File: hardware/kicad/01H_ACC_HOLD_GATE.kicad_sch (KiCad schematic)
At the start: 17 parts, among them Q912 MMBT5551, Q914 PMBT5551,215, Q915 MMBT5401-7-F, U911 140356145000 HOLD

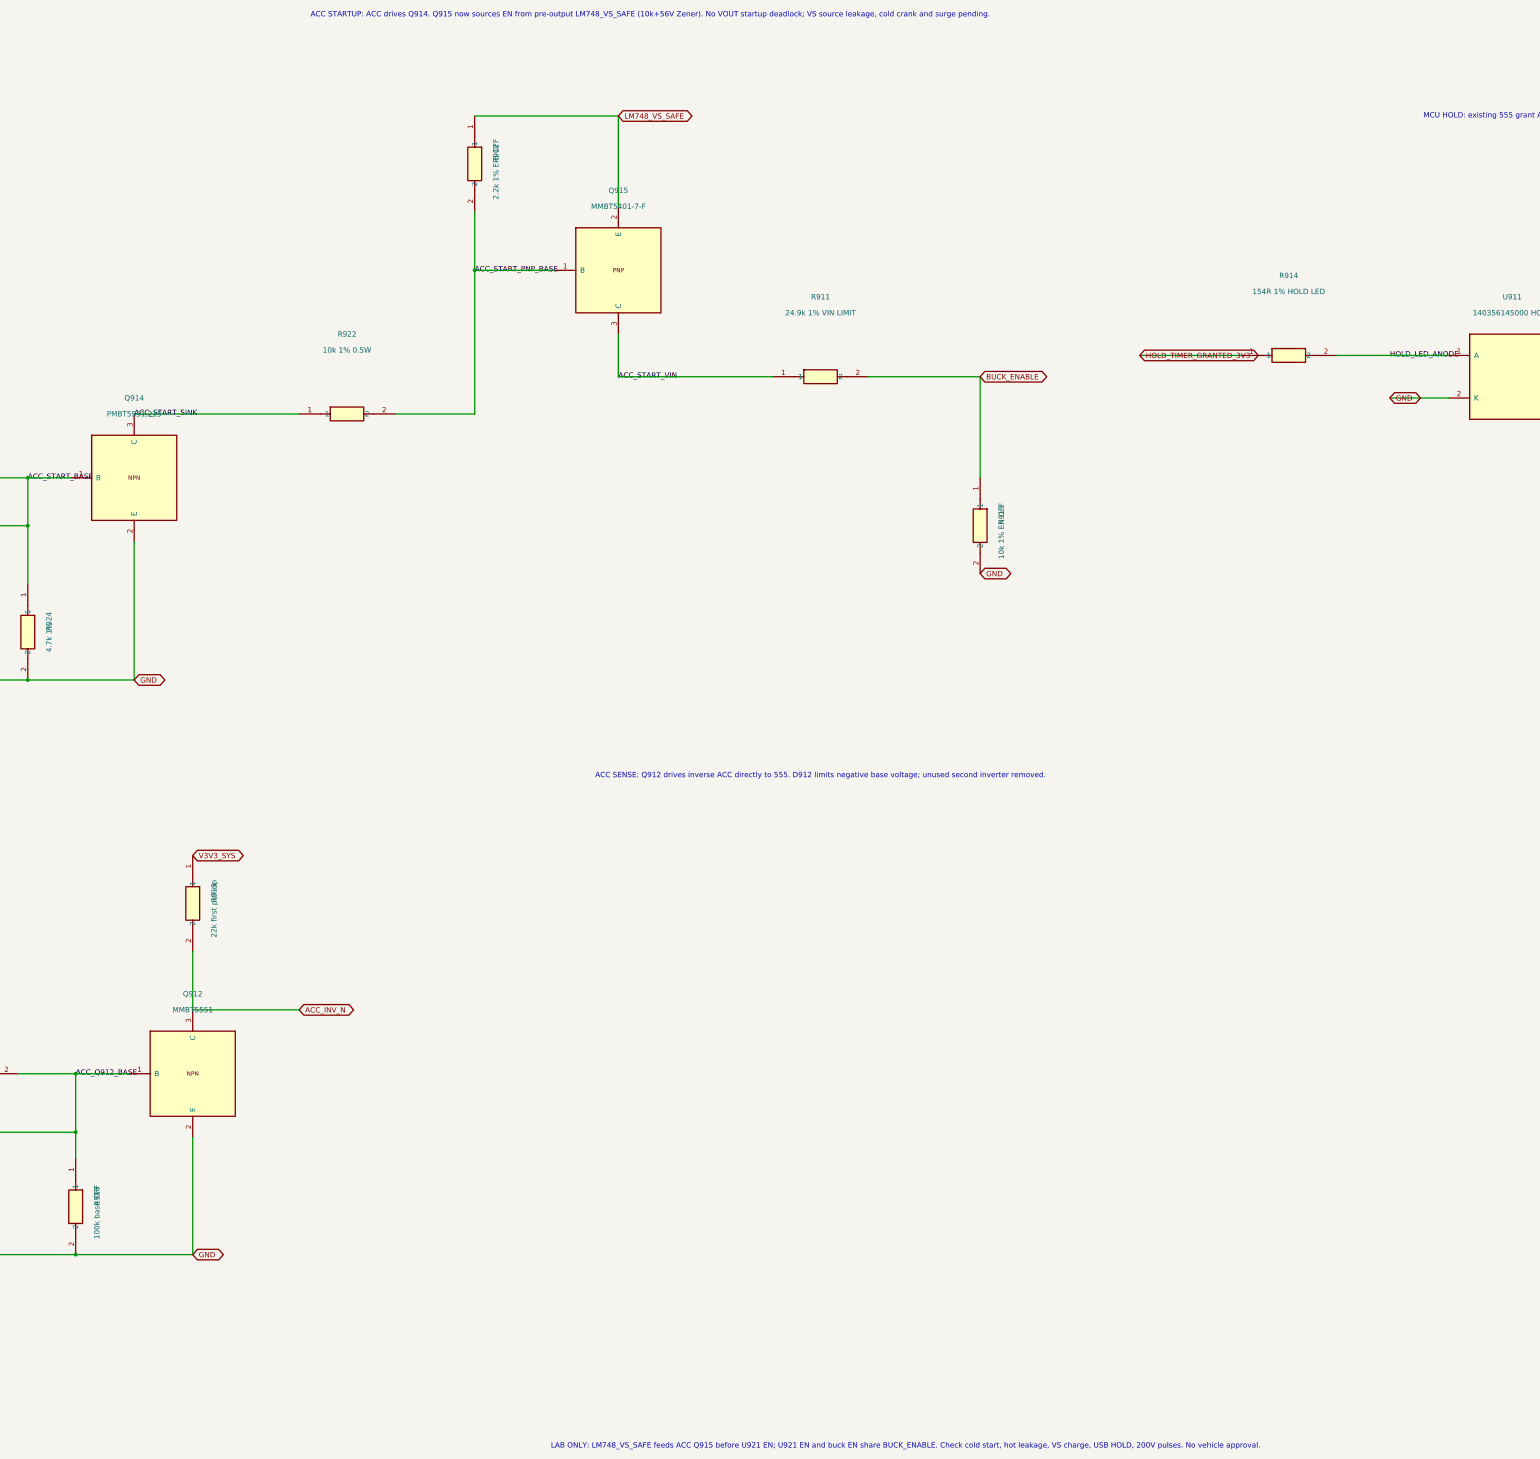
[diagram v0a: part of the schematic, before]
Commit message: hardware(acc): reduce early 9V LM748 VS bias load with 100k/100k PNP drive and 33k/47k EN divider; no shared Buck EN
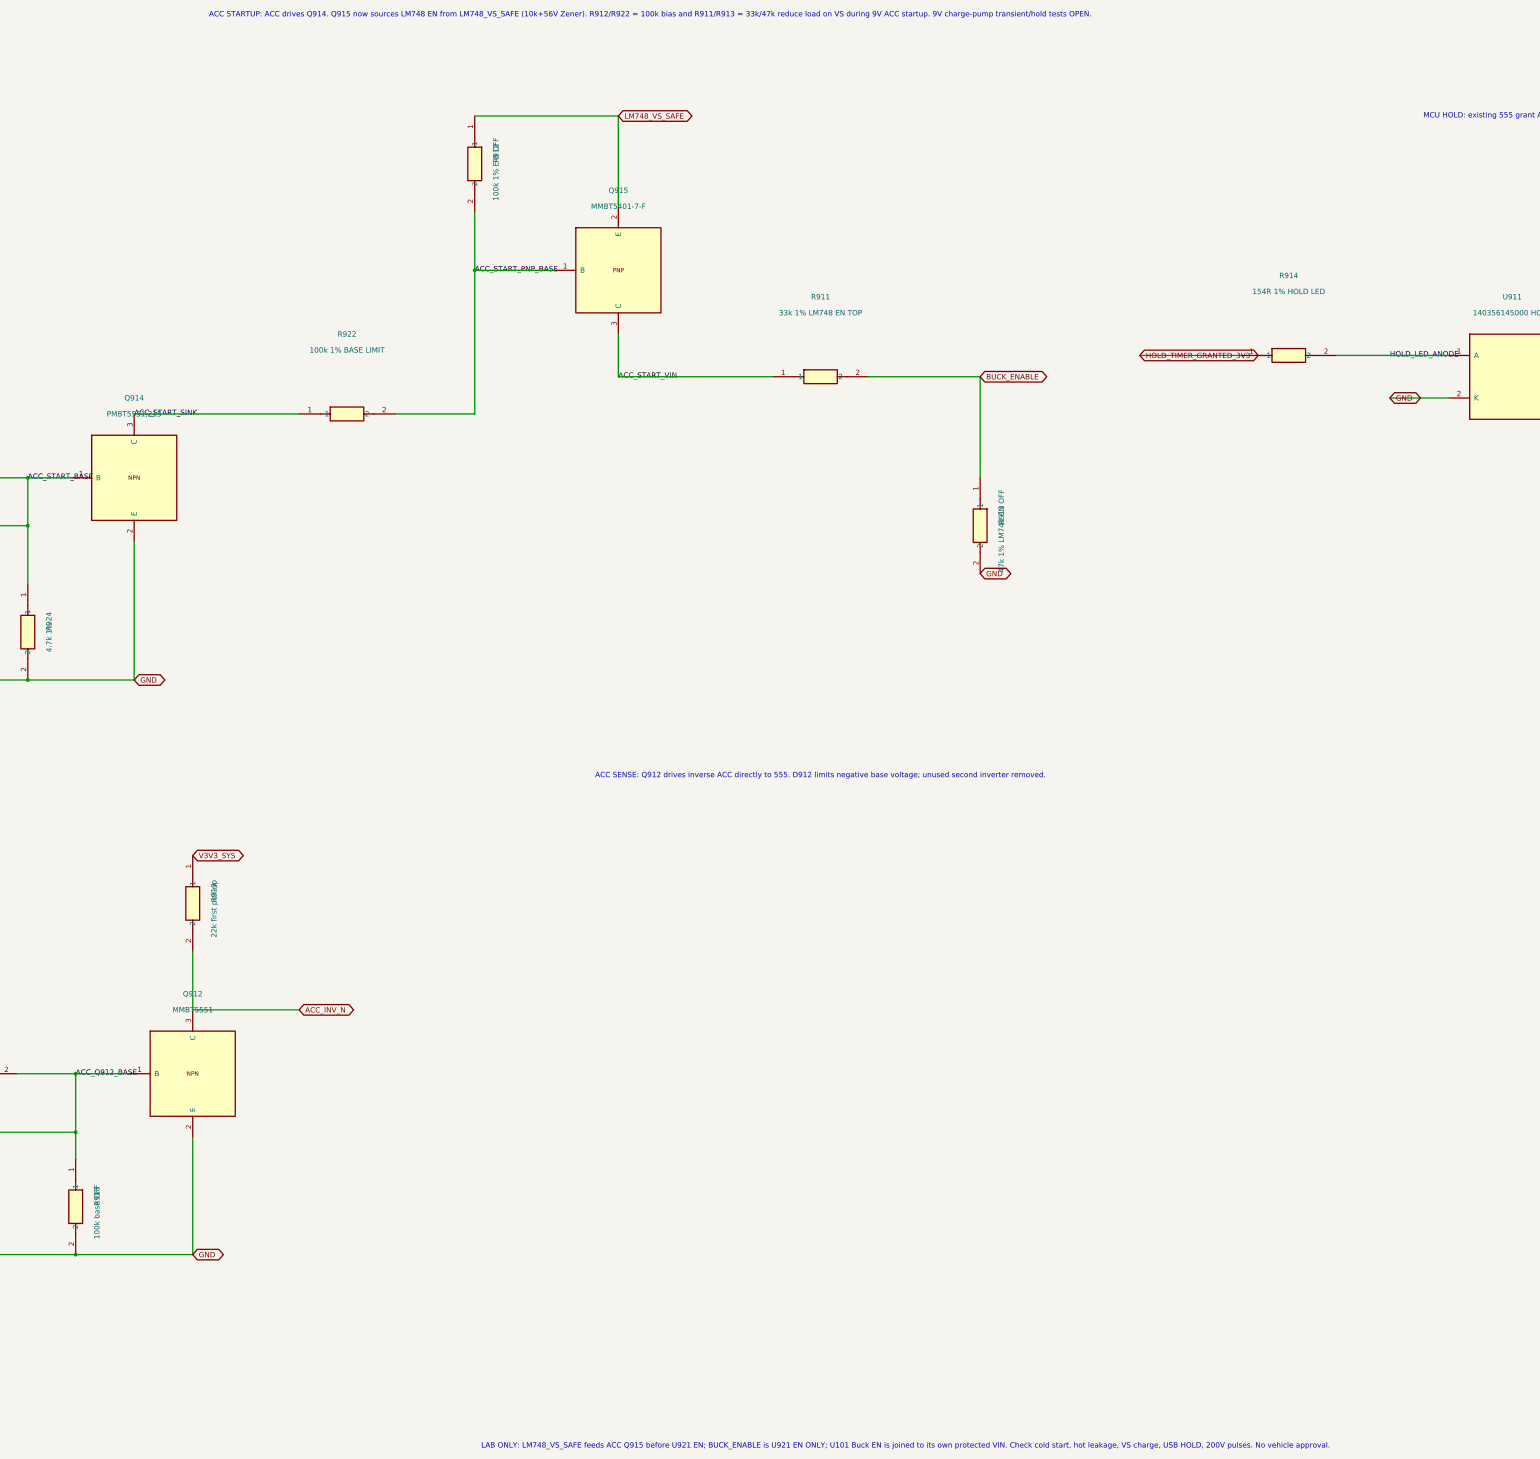
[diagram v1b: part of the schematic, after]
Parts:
- R911: value 24.9k 1% VIN LIMIT -> 33k 1% LM748 EN TOP; MPN (none) -> RC1206FR-0733KL
- R912: value 2.2k 1% E-B OFF -> 100k 1% E-B OFF; MPN (none) -> RC1206FR-07100KL
- R913: value 10k 1% EN OFF -> 47k 1% LM748 EN OFF; MPN (none) -> RC1206FR-0747KL
- R922: value 10k 1% 0.5W -> 100k 1% BASE LIMIT
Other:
- note added: "ACC STARTUP: ACC drives Q914. Q915 now sources LM748 EN from LM748_VS_SAFE (10k+56V Zener). R912/R922 = 100k bias and R911/R913 = 33k/47k reduce load on VS during 9V ACC startup. 9V charge-pump transient/hold tests OPEN."
- note added: "LAB ONLY: LM748_VS_SAFE feeds ACC Q915 before U921 EN; BUCK_ENABLE is U921 EN ONLY; U101 Buck EN is joined to its own protected VIN. Check cold start, hot leakage, VS charge, USB HOLD, 200V pulses. No vehicle approval."
- note removed: "ACC STARTUP: ACC drives Q914. Q915 now sources EN from pre-output LM748_VS_SAFE (10k+56V Zener). No VOUT startup deadlock; VS source leakage, cold crank and surge pending."
- note removed: "LAB ONLY: LM748_VS_SAFE feeds ACC Q915 before U921 EN; U921 EN and buck EN share BUCK_ENABLE. Check cold start, hot leakage, VS charge, USB HOLD, 200V pulses. No vehicle approval."
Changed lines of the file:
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@@
 (kicad_sch (version 20250114) (generator "eeschema") (paper "A2")
 (title_block (title "TripTracer ACC startup referenced to buck VIN / bounded MCU HOLD") (date "2026-10-14") (rev "c0 electrical correction / LAB ONLY"))
-(text "ACC STARTUP: ACC drives Q914. Q915 now sources EN from pre-output LM748_VS_SAFE (10k+56V Zener). No VOUT startup deadlock; VS source leakage, cold crank and surge pending." (at 223.52 24.13 0) (effects (font (size 1.27 1.27))))
+(text "ACC STARTUP: ACC drives Q914. Q915 now sources LM748 EN from LM748_VS_SAFE (10k+56V Zener). R912/R922 = 100k bias and R911/R913 = 33k/47k reduce load on VS during 9V ACC startup. 9V charge-pump transient/hold tests OPEN." (at 223.52 24.13 0) (effects (font (size 1.27 1.27))))
 (symbol (lib_id "TripTracer_V1:PMBT5551_ACC") (at 100.33 134.62 0) (unit 1) (in_bom yes) (on_board yes) (dnp no)
 (property "Reference" "Q914" (at 100.33 115.57 0) (effects (font (size 1.27 1.27))))
@@
 (symbol (lib_id "Tripmaster_Sym:R") (at 151.13 119.38 0) (unit 1) (in_bom yes) (on_board yes) (dnp no)
 (property "Reference" "R922" (at 151.13 100.33 0) (effects (font (size 1.27 1.27))))
-(property "Value" "10k 1% 0.5W" (at 151.13 104.14 0) (effects (font (size 1.27 1.27))))
+(property "Value" "100k 1% BASE LIMIT" (at 151.13 104.14 0) (effects (font (size 1.27 1.27))))
 (property "MPN" "ERJP08F1002V" (at 0 0 0) (effects (font (size 1.27 1.27)) (hide yes)))
 (property "Footprint" "Tripmaster:R_1206_3216" (at 151.13 119.38 0) (effects (font (size 1.27 1.27)) (hide yes)))
@@
 (symbol (lib_id "Tripmaster_Sym:R") (at 181.61 59.69 270) (unit 1) (in_bom yes) (on_board yes) (dnp no)
 (property "Reference" "R912" (at 186.69 57.15 0) (effects (font (size 1.27 1.27))))
-(property "Value" "2.2k 1% E-B OFF" (at 186.69 60.96 0) (effects (font (size 1.27 1.27))))
-(property "Footprint" "Tripmaster:R_1206_3216" (at 181.61 59.69 0) (effects (font (size 1.27 1.27)) (hide yes)))
+(property "Value" "100k 1% E-B OFF" (at 186.69 60.96 0) (effects (font (size 1.27 1.27))))
+(property "MPN" "RC1206FR-07100KL" (at 0 0 0) (effects (font (size 1.27 1.27)) (hide yes))) (property "Footprint" "Tripmaster:R_1206_3216" (at 181.61 59.69 0) (effects (font (size 1.27 1.27)) (hide yes)))
 (pin "1")
 (pin "2")
@@
 (symbol (lib_id "Tripmaster_Sym:R") (at 264.16 110.49 0) (unit 1) (in_bom yes) (on_board yes) (dnp no)
 (property "Reference" "R911" (at 264.16 91.44 0) (effects (font (size 1.27 1.27))))
-(property "Value" "24.9k 1% VIN LIMIT" (at 264.16 95.25 0) (effects (font (size 1.27 1.27))))
-(property "Footprint" "Tripmaster:R_1206_3216" (at 264.16 110.49 0) (effects (font (size 1.27 1.27)) (hide yes)))
+(property "Value" "33k 1% LM748 EN TOP" (at 264.16 95.25 0) (effects (font (size 1.27 1.27))))
+(property "MPN" "RC1206FR-0733KL" (at 0 0 0) (effects (font (size 1.27 1.27)) (hide yes))) (property "Footprint" "Tripmaster:R_1206_3216" (at 264.16 110.49 0) (effects (font (size 1.27 1.27)) (hide yes)))
 (pin "1")
 (pin "2")
@@
 (symbol (lib_id "Tripmaster_Sym:R") (at 302.26 146.05 270) (unit 1) (in_bom yes) (on_board yes) (dnp no)
 (property "Reference" "R913" (at 307.34 143.51 0) (effects (font (size 1.27 1.27))))
-(property "Value" "10k 1% EN OFF" (at 307.34 147.32 0) (effects (font (size 1.27 1.27))))
-(property "Footprint" "Tripmaster:R_1206_3216" (at 302.26 146.05 0) (effects (font (size 1.27 1.27)) (hide yes)))
+(property "Value" "47k 1% LM748 EN OFF" (at 307.34 147.32 0) (effects (font (size 1.27 1.27))))
+(property "MPN" "RC1206FR-0747KL" (at 0 0 0) (effects (font (size 1.27 1.27)) (hide yes))) (property "Footprint" "Tripmaster:R_1206_3216" (at 302.26 146.05 0) (effects (font (size 1.27 1.27)) (hide yes)))
 (pin "1")
 (pin "2")
@@
 (wire (pts (xy 114.3 261.62) (xy 139.7 261.62)) (stroke (width 0) (type default)))
 (global_label "ACC_INV_N" (shape bidirectional) (at 139.7 261.62 0) (effects (font (size 1.27 1.27))))
-(text "LAB ONLY: LM748_VS_SAFE feeds ACC Q915 before U921 EN; U921 EN and buck EN share BUCK_ENABLE. Check cold start, hot leakage, VS charge, USB HOLD, 200V pulses. No vehicle approval." (at 284.48 365.76 0) (effects (font (size 1.27 1.27))))
+(text "LAB ONLY: LM748_VS_SAFE feeds ACC Q915 before U921 EN; BUCK_ENABLE is U921 EN ONLY; U101 Buck EN is joined to its own protected VIN. Check cold start, hot leakage, VS charge, USB HOLD, 200V pulses. No vehicle approval." (at 284.48 365.76 0) (effects (font (size 1.27 1.27))))
 (sheet_instances (path "/" (page "1")))
 (symbol (lib_id "TripTracer_V1:BAT54WS_CLAMP") (at 60.96 308.61 90) (unit 1) (in_bom yes) (on_board yes) (dnp no)

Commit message: bom(acc): correct R922 100k replacement manufacturer MPN; remove previous 10k MPN
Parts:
- R922: MPN ERJP08F1002V -> RC1206FR-07100KL
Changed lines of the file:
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@@
 (property "Reference" "R922" (at 151.13 100.33 0) (effects (font (size 1.27 1.27))))
 (property "Value" "100k 1% BASE LIMIT" (at 151.13 104.14 0) (effects (font (size 1.27 1.27))))
-(property "MPN" "ERJP08F1002V" (at 0 0 0) (effects (font (size 1.27 1.27)) (hide yes)))
+(property "MPN" "RC1206FR-07100KL" (at 0 0 0) (effects (font (size 1.27 1.27)) (hide yes)))
 (property "Footprint" "Tripmaster:R_1206_3216" (at 151.13 119.38 0) (effects (font (size 1.27 1.27)) (hide yes)))
 (pin "1")

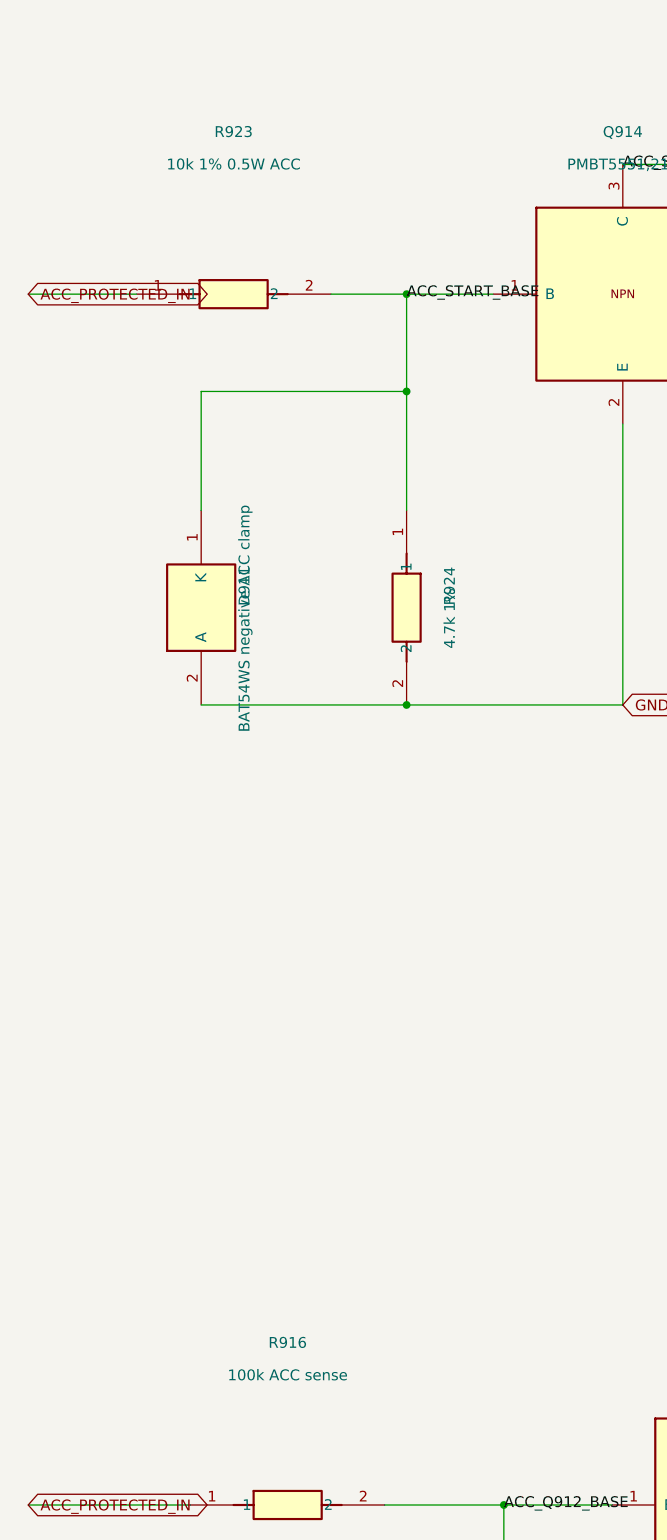
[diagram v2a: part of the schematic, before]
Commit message: hardware(safety): limit ACC 200V transient dissipation with 100k high-pulse R923/R916, 100k Q914 base off; retain 9V drive
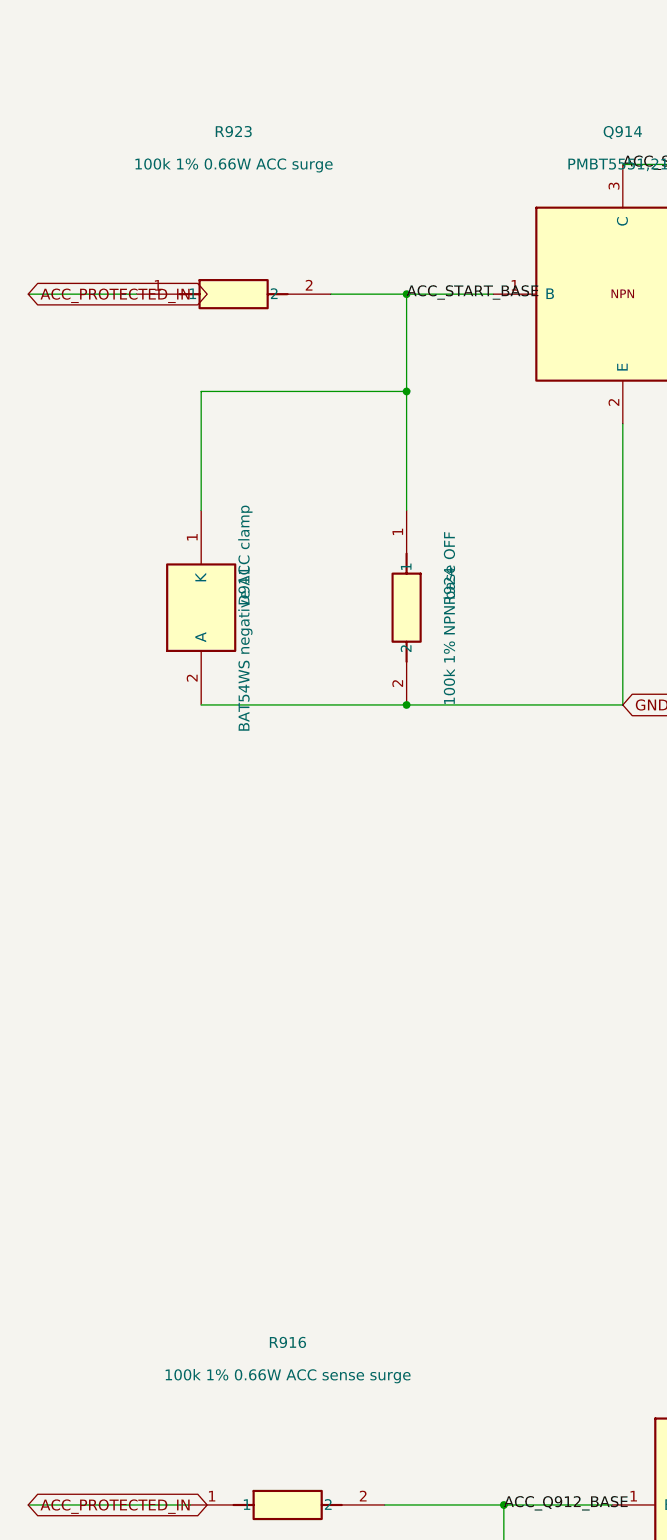
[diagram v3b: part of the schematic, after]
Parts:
- R916: value 100k ACC sense -> 100k 1% 0.66W ACC sense surge; MPN (none) -> ERJP08F1003V
- R923: value 10k 1% 0.5W ACC -> 100k 1% 0.66W ACC surge; MPN ERJP08F1002V -> ERJP08F1003V
- R924: value 4.7k 1% -> 100k 1% NPN base OFF; MPN ERJP08F4701V -> RC1206FR-07100KL
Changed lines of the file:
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@@
 (symbol (lib_id "Tripmaster_Sym:R") (at 54.61 134.62 0) (unit 1) (in_bom yes) (on_board yes) (dnp no)
 (property "Reference" "R923" (at 54.61 115.57 0) (effects (font (size 1.27 1.27))))
-(property "Value" "10k 1% 0.5W ACC" (at 54.61 119.38 0) (effects (font (size 1.27 1.27))))
-(property "MPN" "ERJP08F1002V" (at 0 0 0) (effects (font (size 1.27 1.27)) (hide yes)))
+(property "Value" "100k 1% 0.66W ACC surge" (at 54.61 119.38 0) (effects (font (size 1.27 1.27))))
+(property "MPN" "ERJP08F1003V" (at 0 0 0) (effects (font (size 1.27 1.27)) (hide yes)))
 (property "Footprint" "Tripmaster:R_1206_3216" (at 54.61 134.62 0) (effects (font (size 1.27 1.27)) (hide yes)))
 (pin "1")
@@
 (symbol (lib_id "Tripmaster_Sym:R") (at 74.93 171.45 270) (unit 1) (in_bom yes) (on_board yes) (dnp no)
 (property "Reference" "R924" (at 80.01 168.91 0) (effects (font (size 1.27 1.27))))
-(property "Value" "4.7k 1%" (at 80.01 172.72 0) (effects (font (size 1.27 1.27))))
-(property "MPN" "ERJP08F4701V" (at 0 0 0) (effects (font (size 1.27 1.27)) (hide yes)))
+(property "Value" "100k 1% NPN base OFF" (at 80.01 172.72 0) (effects (font (size 1.27 1.27))))
+(property "MPN" "RC1206FR-07100KL" (at 0 0 0) (effects (font (size 1.27 1.27)) (hide yes)))
 (property "Footprint" "Tripmaster:R_1206_3216" (at 74.93 171.45 0) (effects (font (size 1.27 1.27)) (hide yes)))
 (pin "1")
@@
 (symbol (lib_id "Tripmaster_Sym:R") (at 60.96 276.86 0) (unit 1) (in_bom yes) (on_board yes) (dnp no)
 (property "Reference" "R916" (at 60.96 257.81 0) (effects (font (size 1.27 1.27))))
-(property "Value" "100k ACC sense" (at 60.96 261.62 0) (effects (font (size 1.27 1.27))))
+(property "Value" "100k 1% 0.66W ACC sense surge" (at 60.96 261.62 0) (effects (font (size 1.27 1.27))))
+(property "MPN" "ERJP08F1003V" (at 0 0 0) (effects (font (size 1.27 1.27)) (hide yes)))
 (property "Footprint" "Tripmaster:R_1206_3216" (at 60.96 276.86 0) (effects (font (size 1.27 1.27)) (hide yes)))
 (pin "1")
